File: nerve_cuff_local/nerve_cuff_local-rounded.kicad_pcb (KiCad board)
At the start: 2 copper layers, 4 x 5.3 mm, 2 parts

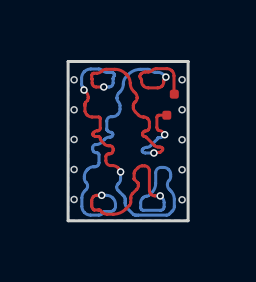
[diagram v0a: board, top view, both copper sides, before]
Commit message: updating clearances for xy gradient board
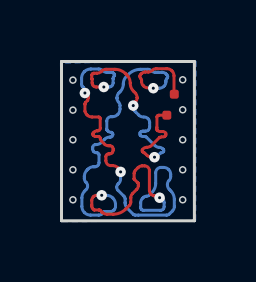
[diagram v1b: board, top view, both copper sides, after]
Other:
- board size 4 x 5.3 mm -> 4.4 x 5.3 mm
